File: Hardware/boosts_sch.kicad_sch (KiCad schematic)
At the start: 47 parts, among them IC1 TPS61089RNRR, IC2 AP2205-W5-7, IC3 AP2205-W5-7, IC4 TPS61089RNRR

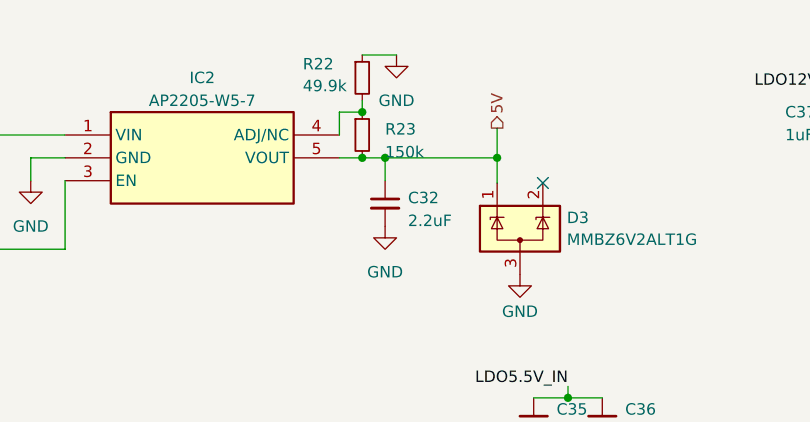
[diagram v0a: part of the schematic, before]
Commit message: changed R23 to match stark
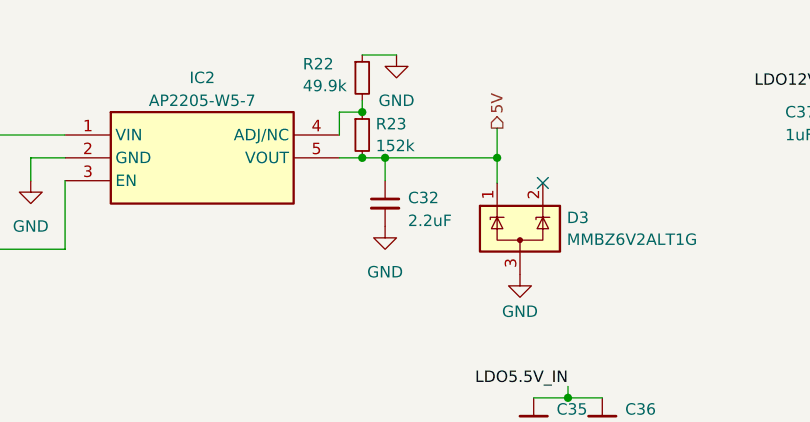
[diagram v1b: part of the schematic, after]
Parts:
- R23: value 150k -> 152k
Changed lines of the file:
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@@
 		(fields_autoplaced yes)
 		(property "Reference" "R23"
-			(at 107.442 45.847 0)
+			(at 106.4006 45.2698 0)
 			(effects
 				(font
@@
 			)
 		)
-		(property "Value" "150k"
-			(at 107.442 48.387 0)
+		(property "Value" "152k"
+			(at 106.4006 47.6941 0)
 			(effects
 				(font

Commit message: post Andrei review, new SD
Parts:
- R28: value 49.9 -> 49.9k
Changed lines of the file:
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@@
 			)
 		)
-		(property "Value" "49.9"
+		(property "Value" "49.9k"
 			(at 204.216 37.2223 0)
 			(effects

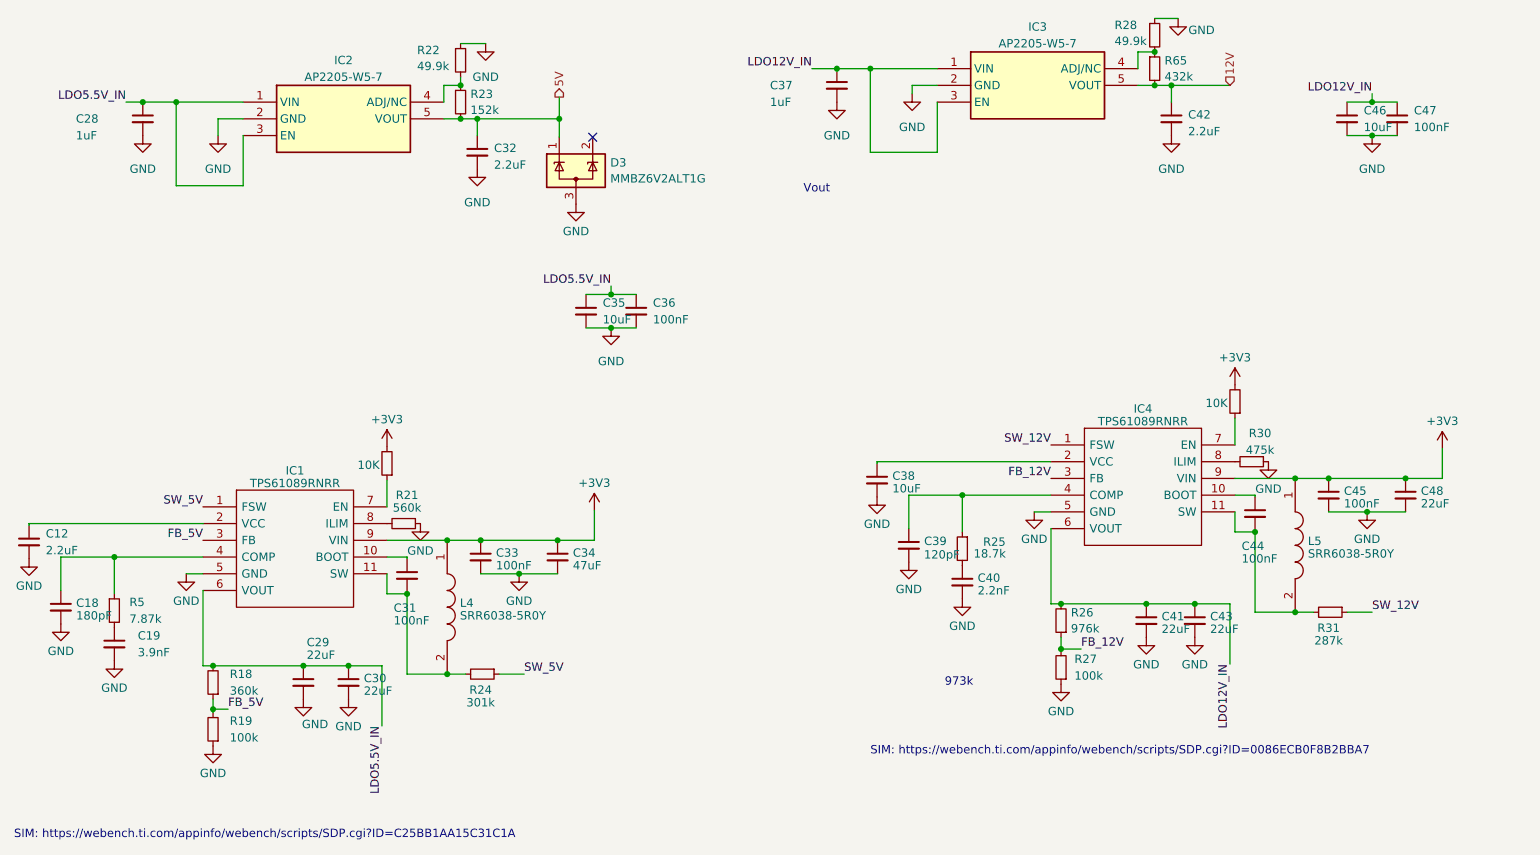
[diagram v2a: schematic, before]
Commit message: non-standard resistor change on 5V ldo
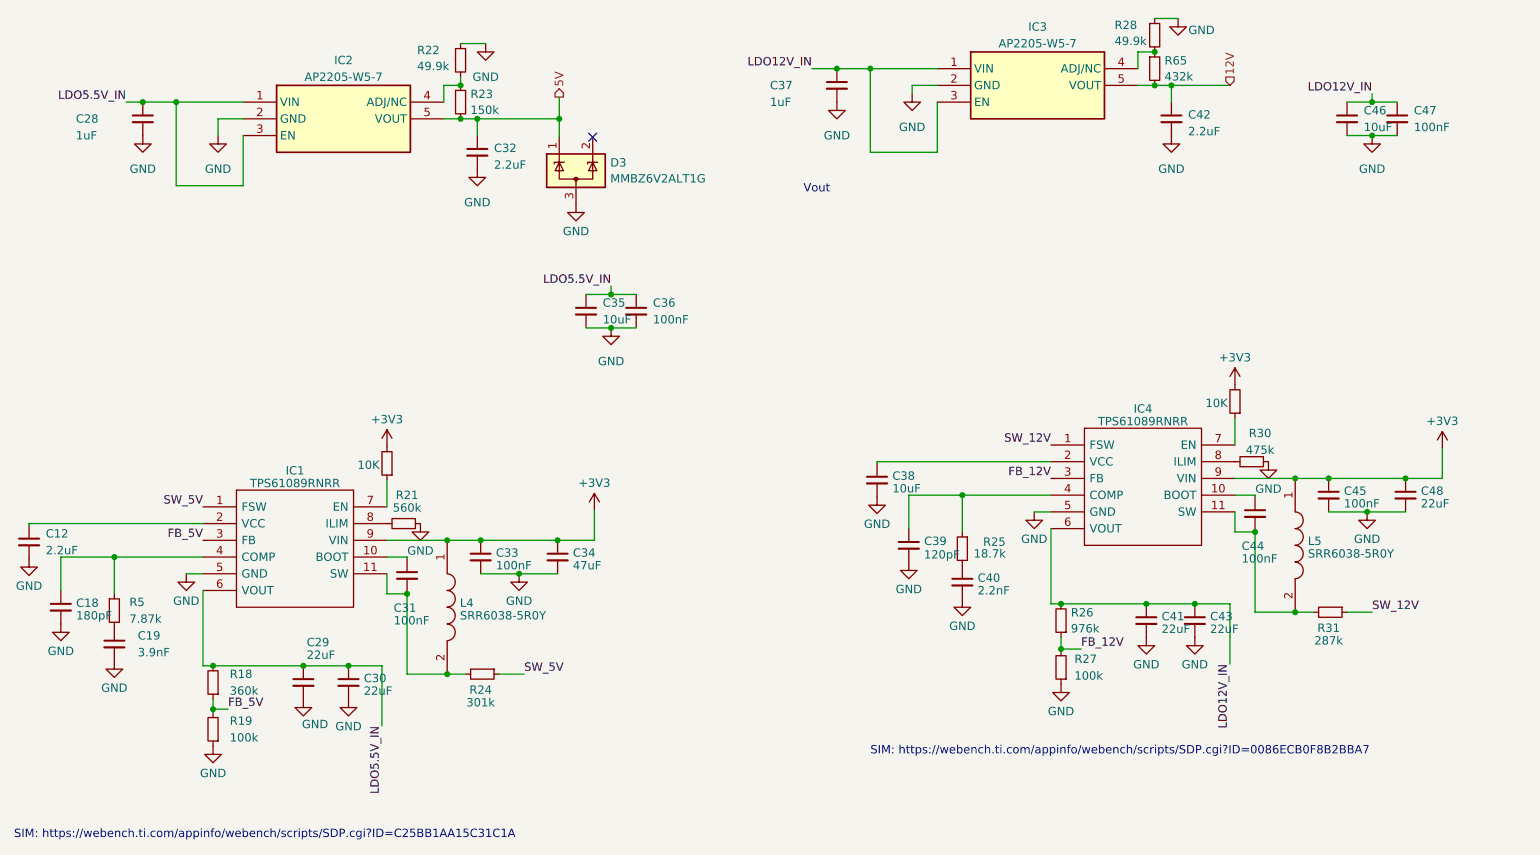
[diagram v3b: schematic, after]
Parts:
- R23: value 152k -> 150k
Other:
- note removed: "973k"
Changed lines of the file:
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@@
 		)
 	)
-	(text "973k\n"
-		(exclude_from_sim no)
-		(at 180.594 134.62 0)
-		(effects
-			(font
-				(size 1.27 1.27)
-			)
-		)
-	)
 	(text "SIM: https://webench.ti.com/appinfo/webench/scripts/SDP.cgi?ID=0086ECB0F8B2BBA7"
 		(exclude_from_sim no)
@@
 			)
 		)
-		(property "Value" "152k"
+		(property "Value" "150k"
 			(at 106.4006 47.6941 0)
 			(effects

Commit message: tidy up schematic and bom
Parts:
- R301: renamed from R5; value 7.87k -> 7.87kΩ
- R302: renamed from R18; value 360k -> 360kΩ
- R303: renamed from R19; value 100k -> 100kΩ
- R304: renamed from R20; value 10K -> 10kΩ
- R305: renamed from R21; value 560k -> 560kΩ
- R306: renamed from R22; value 49.9k -> 49.9kΩ
- R307: renamed from R23; value 150k -> 150kΩ
- R308: renamed from R24; value 301k -> 301kΩ
- R309: renamed from R25; value 18.7k -> 18.7kΩ
- R310: renamed from R26; value 976k -> 976kΩ
- R311: renamed from R27; value 100k -> 100kΩ
- R312: renamed from R28; value 49.9k -> 49.9kΩ
- R313: renamed from R65; value 432k -> 432kΩ
- R314: renamed from R29; value 10K -> 10kΩ
- R315: renamed from R30; value 475k -> 475kΩ
- R316: renamed from R31; value 287k -> 287kΩ
- renumbered C12 to C301, C18 to C302, C19 to C303, C28 to C304, C29 to C305, C30 to C306, C31 to C307, C32 to C308, C33 to C309, C34 to C310, C35 to C311, C36 to C312, C37 to C313, C38 to C314, C39 to C315, C40 to C316, C41 to C317, C42 to C318, C43 to C319, C44 to C320, C45 to C321, C46 to C322, C47 to C323, C48 to C324, D3 to D301, L4 to L301, L5 to L302, IC1 to U301, IC2 to U302, IC3 to U303, IC4 to U304

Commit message: continued
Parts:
- L301, L302: value SRR6038-5R0Y -> 5uH
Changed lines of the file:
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@@
 			)
 		)
-		(property "Value" "SRR6038-5R0Y"
+		(property "Value" "5uH"
 			(at 233.5794 115.0693 90)
 			(effects
@@
 			)
 		)
-		(property "Value" "SRR6038-5R0Y"
+		(property "Value" "5uH"
 			(at 104.8014 124.4673 90)
 			(effects
